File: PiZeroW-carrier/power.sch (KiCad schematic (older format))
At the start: 8 parts, among them CON1 BARREL_JACK, SW1 SW_PUSH, U1 BA50BC0WFP-E2CT, U2 BA06CC0WFP-E2CT

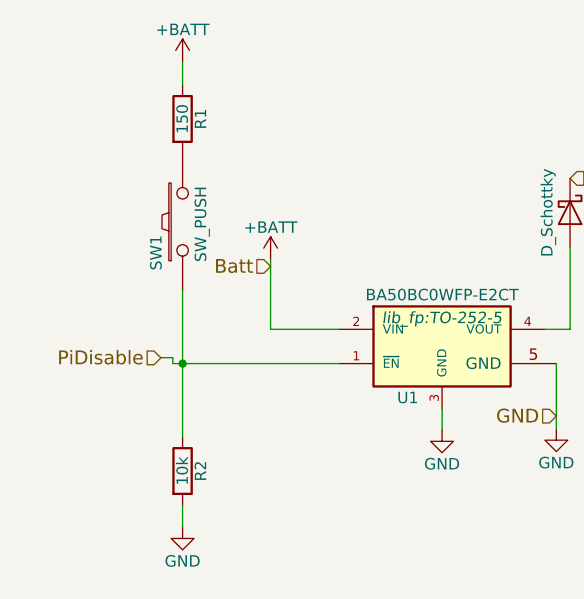
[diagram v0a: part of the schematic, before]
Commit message: PCb Now with PIDisable and 6V Connection.
Featuring a PCB With proper PIDisable and 6V Connections
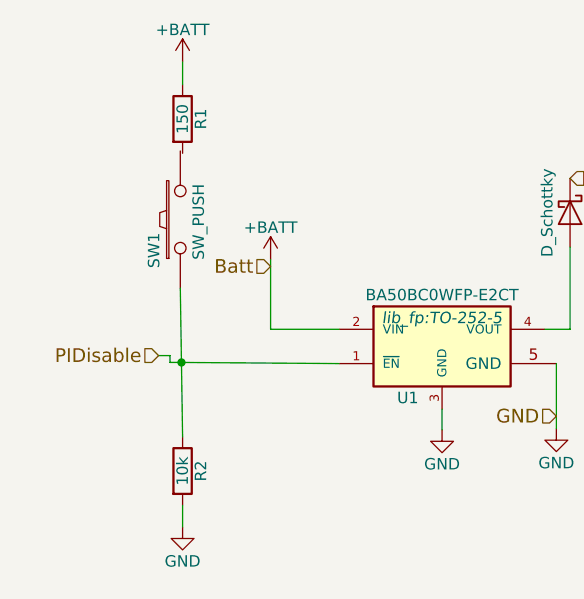
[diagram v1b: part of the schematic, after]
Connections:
- net labels added: PIDisable
- net labels removed: PiDisable
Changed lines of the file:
@@
 	1    0    0    -1
 $EndComp
-Wire Wire Line
-	8015 2240 8015 2545
-Wire Wire Line
-	8015 2545 8315 2545
-Wire Wire Line
-	7630 2695 8315 2695
-Wire Wire Line
-	7630 2695 7630 2210
 $Comp
 L GND #PWR02
@@
 	1    0    0    -1
 $EndComp
-Wire Wire Line
-	9265 2695 9265 2980
-Wire Wire Line
-	8765 2895 8765 2985
-Wire Wire Line
-	9215 2545 9330 2545
-Wire Wire Line
-	9330 2545 9330 2185
 Text HLabel 9330 2185 0    60   Input ~ 0
 +6V
@@
 	1    0    0    -1
 $EndComp
-Wire Wire Line
-	3880 2270 3880 2575
-Wire Wire Line
-	3880 2575 4180 2575
-Wire Wire Line
-	3495 2725 4180 2725
 $Comp
 L GND #PWR05
@@
 	1    0    0    -1
 $EndComp
-Wire Wire Line
-	5130 2725 5130 3010
-Wire Wire Line
-	4630 2925 4630 3015
-Wire Wire Line
-	5080 2575 5190 2575
-Wire Wire Line
-	5190 2575 5190 2215
-Text HLabel 3400 2700 0    60   Input ~ 0
-PiDisable
 Text HLabel 5190 1915 2    60   Input ~ 0
 +5V
@@
 	1    0    0    -1
 $EndComp
-Wire Wire Line
-	7985 2695 7985 2975
-Connection ~ 7985 2695
 $Comp
 L R R1
@@
 	1    0    0    -1
 $EndComp
-Wire Wire Line
-	3495 1405 3495 1505
 $Comp
 L R R2
@@
 L SW_PUSH SW1
 U 1 1 5A258078
-P 3495 2105
-F 0 "SW1" H 3360 2220 50  0000 C CNN
-F 1 "SW_PUSH" H 3485 2025 50  0000 C CNN
-F 2 "Buttons_Switches_SMD:SW_SPST_TL3342" H 3495 2105 50  0001 C CNN
-F 3 "" H 3495 2105 50  0000 C CNN
-	1    3495 2105
+P 3485 2095
+F 0 "SW1" H 3350 2210 50  0000 C CNN
+F 1 "SW_PUSH" H 3475 2015 50  0000 C CNN
+F 2 "Buttons_Switches_SMD:SW_SPST_TL3342" H 3485 2095 50  0001 C CNN
+F 3 "" H 3485 2095 50  0000 C CNN
+	1    3485 2095
 	0    -1   -1   0
 $EndComp
@@
 	1    0    0    -1
 $EndComp
-Wire Wire Line
-	3495 3345 3495 3440
 $Comp
 L +BATT #PWR09
@@
 	1    0    0    -1
 $EndComp
-Wire Wire Line
-	7630 1810 7630 1910
-Wire Wire Line
-	3495 2405 3495 3045
-Connection ~ 3495 2725
 $Comp
 L BARREL_JACK CON1
@@
 	1    0    0    -1
 $EndComp
-Wire Wire Line
-	5870 4940 5870 5135
-Wire Wire Line
-	5705 5040 5870 5040
-Wire Wire Line
-	5705 4940 5870 4940
-Connection ~ 5870 5040
 $Comp
 L +BATT #PWR011
@@
 	1    0    0    -1
 $EndComp
-Wire Wire Line
-	5705 4840 5870 4840
-Wire Wire Line
-	5870 4840 5870 4670
 $Comp
 L D_Schottky D6
@@
 	0    1    1    0
 $EndComp
-Wire Wire Line
-	3401 2699 3452 2699
-Wire Wire Line
-	3452 2699 3452 2725
-Wire Wire Line
-	3452 2725 3494 2725
 Text HLabel 7985 2975 0    60   Input ~ 0
 LEDEnable
+Wire Wire Line
+	8015 2240 8015 2545
+Wire Wire Line
+	8015 2545 8315 2545
+Wire Wire Line
+	7630 2695 8315 2695
+Wire Wire Line
+	7630 2695 7630 2210
+Wire Wire Line
+	9265 2695 9265 2980
+Wire Wire Line
+	8765 2895 8765 2985
+Wire Wire Line
+	9215 2545 9330 2545
+Wire Wire Line
+	9330 2545 9330 2185
+Wire Wire Line
+	3880 2270 3880 2575
+Wire Wire Line
+	3880 2575 4180 2575
+Wire Wire Line
+	3490 2720 4180 2725
+Wire Wire Line
+	5130 2725 5130 3010
+Wire Wire Line
+	4630 2925 4630 3015
+Wire Wire Line
+	5080 2575 5190 2575
+Wire Wire Line
+	5190 2575 5190 2215
+Wire Wire Line
+	7985 2695 7985 2975
+Connection ~ 7985 2695
+Wire Wire Line
+	3495 1405 3495 1505
+Wire Wire Line
+	3495 3345 3495 3440
+Wire Wire Line
+	7630 1810 7630 1910
+Wire Wire Line
+	3485 2395 3495 3045
+Connection ~ 3490 2720
+Wire Wire Line
+	5870 4940 5870 5135
+Wire Wire Line
+	5705 5040 5870 5040
+Wire Wire Line
+	5705 4940 5870 4940
+Connection ~ 5870 5040
+Wire Wire Line
+	5705 4840 5870 4840
+Wire Wire Line
+	5870 4840 5870 4670
+Wire Wire Line
+	3490 2720 3440 2720
+Wire Wire Line
+	3440 2720 3440 2690
+Wire Wire Line
+	3440 2690 3390 2690
+Text HLabel 3390 2690 0    60   Input ~ 0
+PIDisable
 $EndSCHEMATC
